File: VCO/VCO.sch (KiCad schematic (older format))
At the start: 45 parts, among them J1 Input, J2 Power, J3 Output, J4 PW, Q1 BC807, Q2 BC807, Q3 BC807, SW1 SAW/SQ, U1 LM324A, U2 LM324A

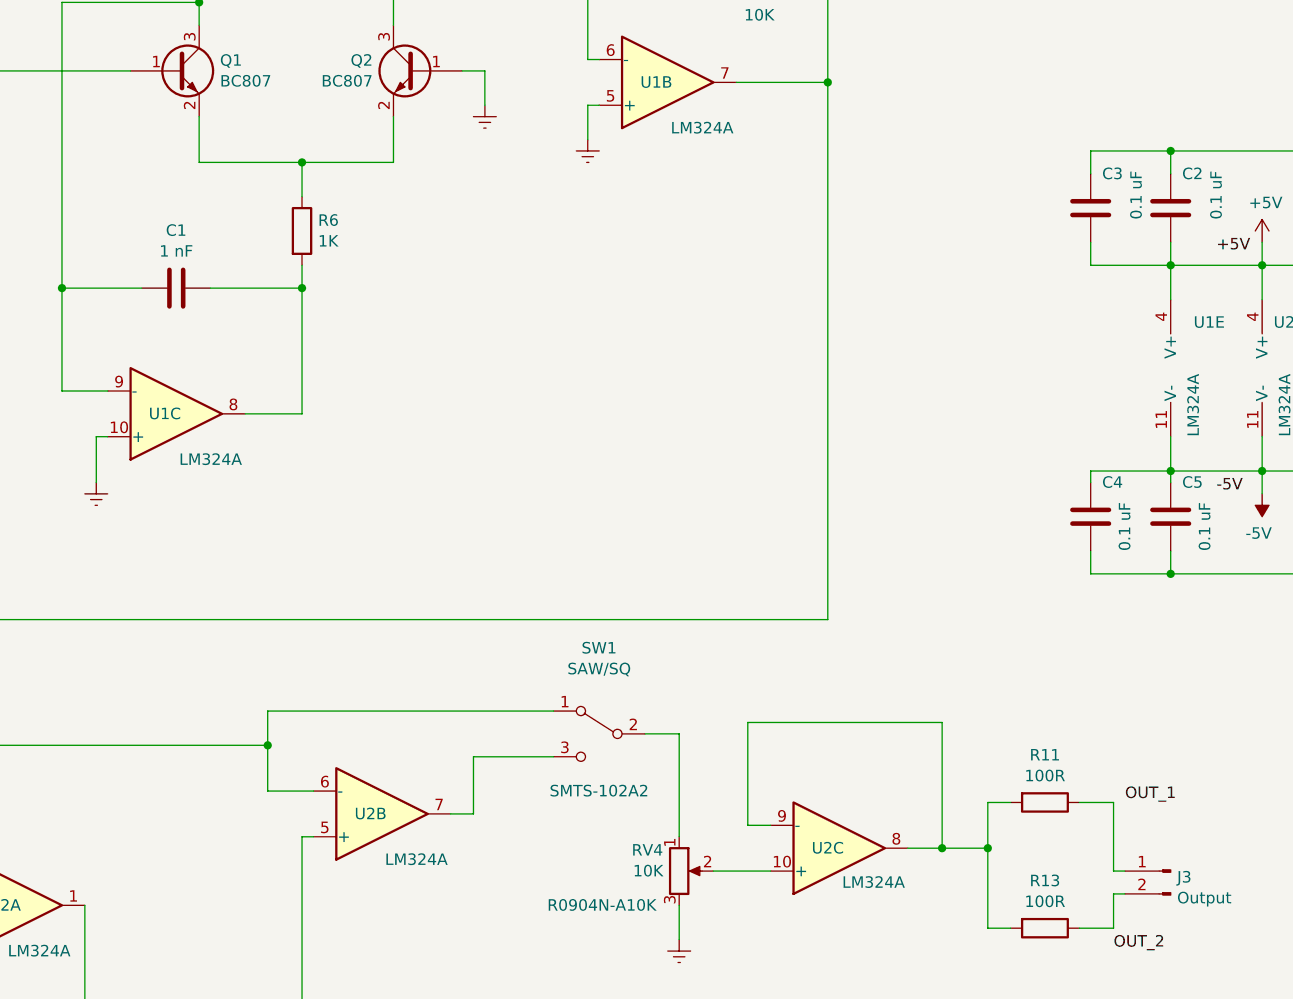
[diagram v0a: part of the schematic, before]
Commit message: New edit schems, add net lists, pcb files and library
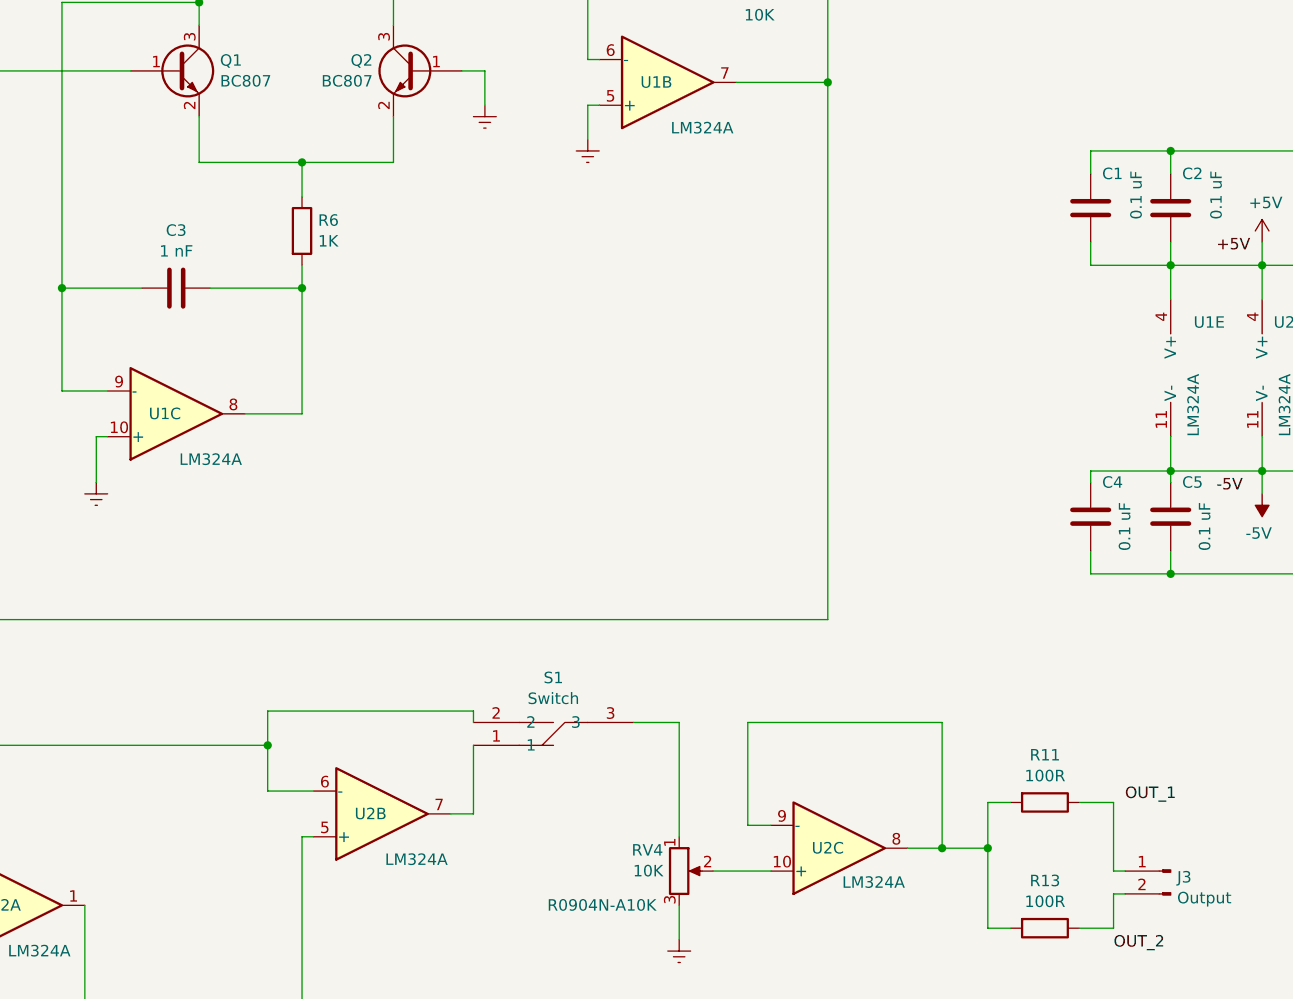
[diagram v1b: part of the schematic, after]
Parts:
- removed SW1: SAW/SQ, M2013SS1W03:M2018SD3G03, symbol Switch:SW_SPDT
- added S1: Switch, M2013SS1W03:M2018SD3G03, symbol M2013SS1W03:Switch
- RV3, RV4, RV5: footprint Potentiometer_THT:Potentiometer_Bourns_PTV09A-1_Single_Vertical -> R0409N:PTV09A4020FB103
- renumbered C3 to C1, C1 to C3
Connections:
- net at C6.1, U1.14, U2.2 (-)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: now also S1.2
- net at U2.7: now also S1.1
- net at RV4.1: now also S1.3
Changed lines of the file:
@@
 F 0 "RV3" H 3130 3096 50  0000 R CNN
 F 1 "10K" H 3100 3000 50  0000 R CNN
-F 2 "Potentiometer_THT:Potentiometer_Bourns_PTV09A-1_Single_Vertical" H 3200 3050 50  0001 C CNN
+F 2 "R0409N:PTV09A4020FB103" H 3200 3050 50  0001 C CNN
 F 3 "~" H 3200 3050 50  0001 C CNN
 F 4 "R0904N-A10K" H 2900 2850 50  0000 C CNN "Тип"
@@
 	-1   0    0    1
 $EndComp
-Wire Wire Line
-	3200 3200 3200 3300
-Wire Wire Line
-	3200 2900 3200 2800
 $Comp
 L Amplifier_Operational:LM324A U1
@@
 $EndComp
 $Comp
-L Device:C C1
+L Device:C C3
 U 1 1 5C6C1557
 P 5200 2450
-F 0 "C1" V 4948 2450 50  0000 C CNN
+F 0 "C3" V 4948 2450 50  0000 C CNN
 F 1 "1 nF" V 5039 2450 50  0000 C CNN
 F 2 "Capacitor_SMD:C_0603_1608Metric" H 5238 2300 50  0001 C CNN
@@
 $EndComp
 $Comp
-L power:+5V #PWR014
+L power:+5V #PWR015
 U 1 1 5C71D4F7
 P 3700 5450
-F 0 "#PWR014" H 3700 5300 50  0001 C CNN
+F 0 "#PWR015" H 3700 5300 50  0001 C CNN
 F 1 "+5V" H 3715 5623 50  0000 C CNN
 F 2 "" H 3700 5450 50  0001 C CNN
@@
 F 0 "RV5" V 5050 6200 50  0000 R CNN
 F 1 "10K" H 5100 5950 50  0000 R CNN
-F 2 "Potentiometer_THT:Potentiometer_Bourns_PTV09A-1_Single_Vertical" H 5150 6150 50  0001 C CNN
+F 2 "R0409N:PTV09A4020FB103" H 5150 6150 50  0001 C CNN
 F 3 "~" H 5150 6150 50  0001 C CNN
 F 4 "R0904N-A10K" V 4900 5950 50  0000 C CNN "Тип"
@@
 Wire Wire Line
 	4600 7000 4550 7000
-$Comp
-L Switch:SW_SPDT SW1
-U 1 1 5C76CF5E
-P 7050 4400
-F 0 "SW1" H 7050 4775 50  0000 C CNN
-F 1 "SAW/SQ" H 7050 4684 50  0000 C CNN
-F 2 "M2013SS1W03:M2018SD3G03" H 7050 4400 50  0001 C CNN
-F 3 "" H 7050 4400 50  0001 C CNN
-F 4 "SMTS-102A2" H 7050 4150 50  0000 C CNN "ТИП"
-	1    7050 4400
-	-1   0    0    -1
-$EndComp
 Wire Wire Line
 	6400 4750 6500 4750
@@
 Connection ~ 5600 4450
 Wire Wire Line
-	5600 4300 6850 4300
-Wire Wire Line
-	6850 4500 6500 4500
-Wire Wire Line
-	6500 4500 6500 4750
+	5600 4300 6500 4300
 $Comp
 L Device:R_POT RV4
@@
 F 0 "RV4" H 7330 5091 50  0000 R CNN
 F 1 "10K" H 7330 5000 50  0000 R CNN
-F 2 "Potentiometer_THT:Potentiometer_Bourns_PTV09A-1_Single_Vertical" H 7400 5000 50  0001 C CNN
+F 2 "R0409N:PTV09A4020FB103" H 7400 5000 50  0001 C CNN
 F 3 "~" H 7400 5000 50  0001 C CNN
 F 4 "R0904N-A10K" H 7300 4850 50  0000 R CNN "Тип"
@@
 $EndComp
 Wire Wire Line
-	7250 4400 7400 4400
-Wire Wire Line
-	7400 4400 7400 4850
-$Comp
-L power:GNDREF #PWR015
+	7400 4350 7400 4850
+$Comp
+L power:GNDREF #PWR014
 U 1 1 5C78BF89
 P 7400 5300
-F 0 "#PWR015" H 7400 5050 50  0001 C CNN
+F 0 "#PWR014" H 7400 5050 50  0001 C CNN
 F 1 "GNDREF" H 7405 5127 50  0001 C CNN
 F 2 "" H 7400 5300 50  0001 C CNN
@@
 Wire Wire Line
 	9550 3250 9550 3100
-Wire Wire Line
-	9950 3100 9950 3250
 Connection ~ 9950 3250
 Wire Wire Line
@@
 $EndComp
 $Comp
-L Device:C C3
+L Device:C C1
 U 1 1 5C7F99E3
 P 9200 2100
-F 0 "C3" H 9250 2250 50  0000 L CNN
+F 0 "C1" H 9250 2250 50  0000 L CNN
 F 1 "0.1 uF" V 9400 2050 50  0000 L CNN
 F 2 "Capacitor_SMD:C_0603_1608Metric" H 9238 1950 50  0001 C CNN
@@
 Wire Wire Line
 	9200 3600 9200 3700
+Wire Wire Line
+	9950 3100 9950 3250
+$Comp
+L M2013SS1W03:Switch S1
+U 1 1 5C753FF1
+P 7200 4350
+F 0 "S1" H 7550 4155 50  0000 C CNN
+F 1 "Switch" H 7550 4246 50  0000 C CNN
+F 2 "M2013SS1W03:M2018SD3G03" V 8450 4400 50  0001 L CNN
+F 3 "https://componentsearchengine.com/Datasheets/1/M2013SS1W03.pdf" H 7850 4350 50  0001 L CNN
+F 4 "NKK SWITCHES - M2013SS1W03 - TOGGLE SWITCH, SPDT, VERT, ON-OFF-ON" H 7850 4250 50  0001 L CNN "Description"
+F 5 "18" H 7850 4150 50  0001 L CNN "Height"
+F 6 "NKK Switches" H 7850 4050 50  0001 L CNN "Manufacturer_Name"
+F 7 "M2013SS1W03" H 7850 3950 50  0001 L CNN "Manufacturer_Part_Number"
+F 8 "70192098" H 7850 3650 50  0001 L CNN "Allied_Number"
+F 9 "https://www.alliedelec.com/nkk-switches-m2013ss1w03/70192098/" H 7850 3550 50  0001 L CNN "Allied Price/Stock"
+F 10 "633-M201303" H 7850 3450 50  0001 L CNN "Mouser Part Number"
+F 11 "https://www.mouser.com/Search/Refine.aspx?Keyword=633-M201303" H 7850 3350 50  0001 L CNN "Mouser Price/Stock"
+	1    7200 4350
+	-1   0    0    1
+$EndComp
+Wire Wire Line
+	6500 4300 6500 4350
+Wire Wire Line
+	6500 4450 6500 4750
+Wire Wire Line
+	7200 4350 7400 4350
+Wire Wire Line
+	3200 3200 3200 3300
+Wire Wire Line
+	3200 2900 3200 2800
 $EndSCHEMATC

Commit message: Изменены библиотеки. Добавлинны библиотеки примененные в проекте локально. Добавленны заготовки для печатных плат. Добавленны 3D модели компоненток.
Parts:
- C1, C2, C3, C4, C5: footprint Capacitor_SMD:C_0603_1608Metric -> footprint:c0603; symbol Device:C -> uRack:C
- C6: footprint Capacitor_SMD:C_0603_1608Metric -> footprint:c0603
- J1, J2: footprint Connector_PinHeader_2.54mm:PinHeader_1x03_P2.54mm_Vertical -> footprint:pls1x03; symbol Connector:Conn_01x03_Male -> uRack:Conn_01x03_Male
- J3: footprint Connector_PinHeader_2.54mm:PinHeader_1x02_P2.54mm_Vertical -> footprint:pls1x02; symbol Connector:Conn_01x02_Male -> uRack:Conn_01x02_Male
- J4: footprint Connector_PinHeader_2.54mm:PinHeader_1x01_P2.54mm_Vertical -> footprint:pls1x01; symbol Connector:Conn_01x01_Male -> uRack:Conn_01x01_Male
- Q1: footprint Package_TO_SOT_SMD:SOT-23 -> footprint:SOT-23
- Q2, Q3: footprint Package_TO_SOT_SMD:SOT-23 -> footprint:SOT-23; symbol Transistor_BJT:BC817 -> uRack:BC817
- R1, R10, R11, R12, R13, R14, R15, R16, R17, R18, R19, R2, R20, R21, R22, R23, R24, R3, R4, R5, R6, R7, R8, R9: footprint Resistor_SMD:R_0603_1608Metric -> footprint:r0603; symbol Device:R -> uRack:R
- RV1, RV2: footprint Potentiometer_THT:Potentiometer_Bourns_3296W_Vertical -> footprint:w3296w; symbol Device:R_POT -> uRack:R_POT
- RV3, RV4, RV5: footprint R0409N:PTV09A4020FB103 -> footprint:PTV09A4020FB103; symbol Device:R_POT -> uRack:R_POT
- S1: footprint M2013SS1W03:M2018SD3G03 -> footprint:smts-102-2a2; symbol M2013SS1W03:Switch -> uRack:Switch
- U1, U2: footprint Package_SO:SOIC-14_3.9x8.7mm_P1.27mm -> footprint:soic-14; symbol Amplifier_Operational:LM324A -> uRack:LM324

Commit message: fix relative path, fix lib path in VCO
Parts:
- C6: symbol Device:C -> uRack:C
- Q1: symbol Transistor_BJT:BC817 -> uRack:BC817
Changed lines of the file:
@@
 EESchema Schematic File Version 4
-LIBS:VCO-cache
 EELAYER 26 0
 EELAYER END
@@
 	4400 1500 4350 1500
 $Comp
-L Transistor_BJT:BC817 Q1
+L uRack:BC817 Q1
 U 1 1 5C6B6D11
 P 5200 1500
@@
 	1650 3900 1650 4950
 $Comp
-L Device:C C6
+L uRack:C C6
 U 1 1 5C6E5337
 P 2950 4450

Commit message: Исправленну ошибки в схемах. Полностью локальные библиотеки и 3D модели.
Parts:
- S1: footprint footprint:smts-102-2a2 -> footprint:smts
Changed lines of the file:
@@
 F 0 "S1" H 7550 4155 50  0000 C CNN
 F 1 "Switch" H 7550 4246 50  0000 C CNN
-F 2 "footprint:smts-102-2a2" V 8450 4400 50  0001 L CNN
+F 2 "footprint:smts" V 8450 4400 50  0001 L CNN
 F 3 "https://componentsearchengine.com/Datasheets/1/M2013SS1W03.pdf" H 7850 4350 50  0001 L CNN
 F 4 "NKK SWITCHES - M2013SS1W03 - TOGGLE SWITCH, SPDT, VERT, ON-OFF-ON" H 7850 4250 50  0001 L CNN "Description"

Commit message: ADD PCB module VCO. ADD folder MOTHEBORD.
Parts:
- removed J2: Power, footprint:pls1x03, symbol uRack:Conn_01x03_Male
- added J1, J11, J2, J4, J5, J6, J7, J8, J9: Conn_01x05_Male, footprint:pls1x05, symbol uRack:Conn_01x05_Male
- renumbered J3 to J10, J4 to J12, J1 to J3
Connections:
- wire segments 182 -> 272
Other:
- moved on the sheet: C1, C2, C4, C5, J10, R11, R13, RV4, U1E, U2C, U2E
